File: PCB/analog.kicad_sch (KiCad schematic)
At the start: 31 parts, among them U4 74HC4051, U5 OPA350, U6 74HC4051, U7 74HC4051

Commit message: Updated sheets
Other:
- company: Cipulot PCB Design  -> LU.SV Solutions
- title: CDS - Analog Circuit -> CDS

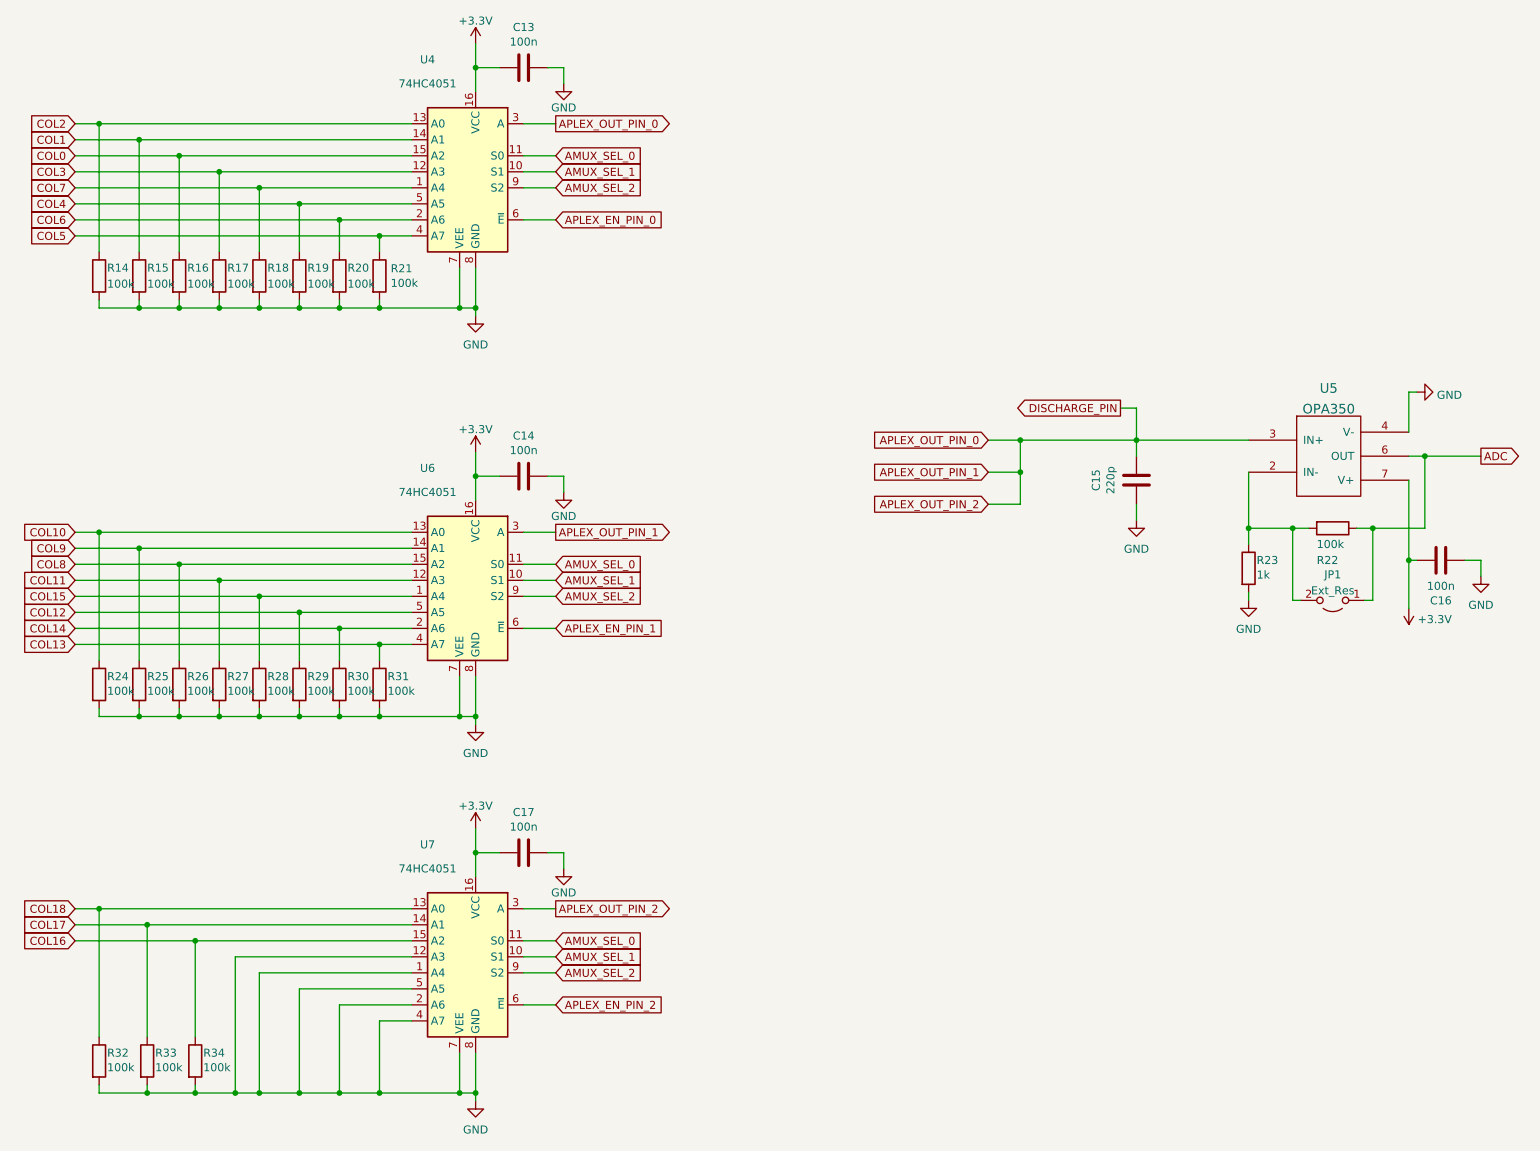
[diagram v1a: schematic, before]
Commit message: Update
Updated the License for the project and relative details.
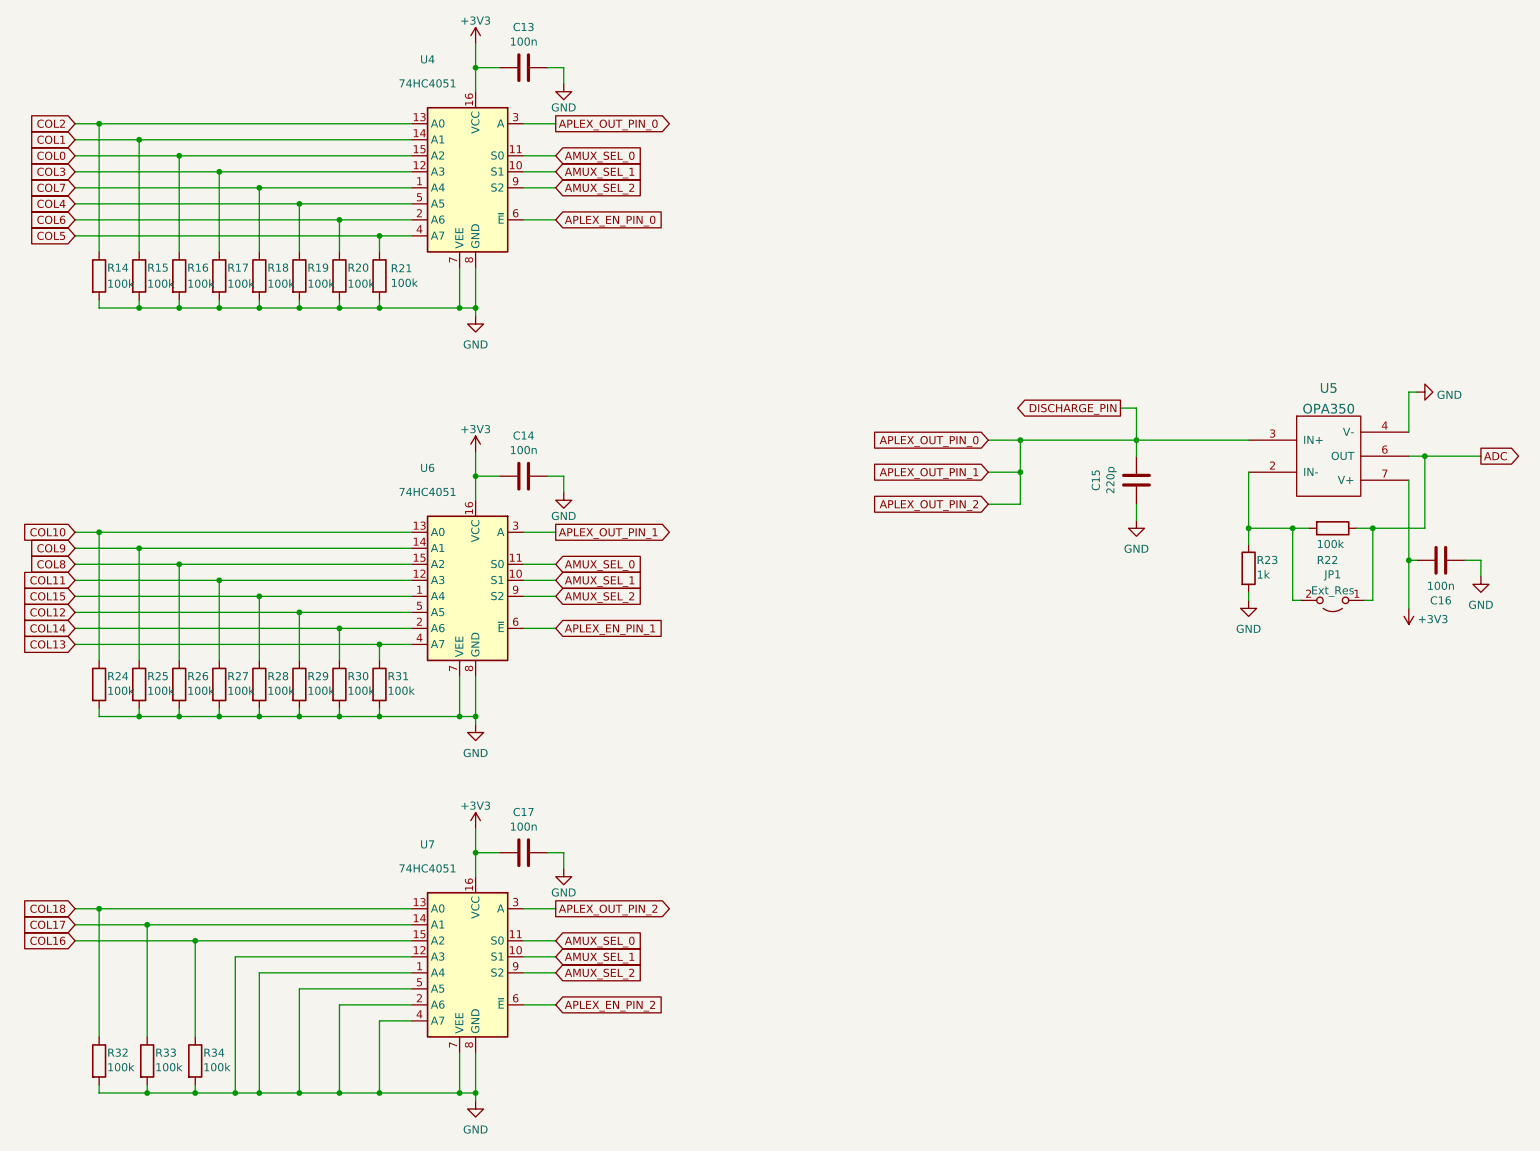
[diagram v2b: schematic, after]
